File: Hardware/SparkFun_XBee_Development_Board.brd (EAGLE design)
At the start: 45.7 x 63.5 mm, 138 parts, among them J1 USB Female Type C Connector, J3 USB Female Type C Connector, J4 QWIIC_RIGHT_ANGLE, Q2 3.1A/30V/105mΩ, U1 FSUSB30MUX_MSOP10, U2 AP63203, U3 ESD Diode, U5 ESD Diode, U7 FT231XS

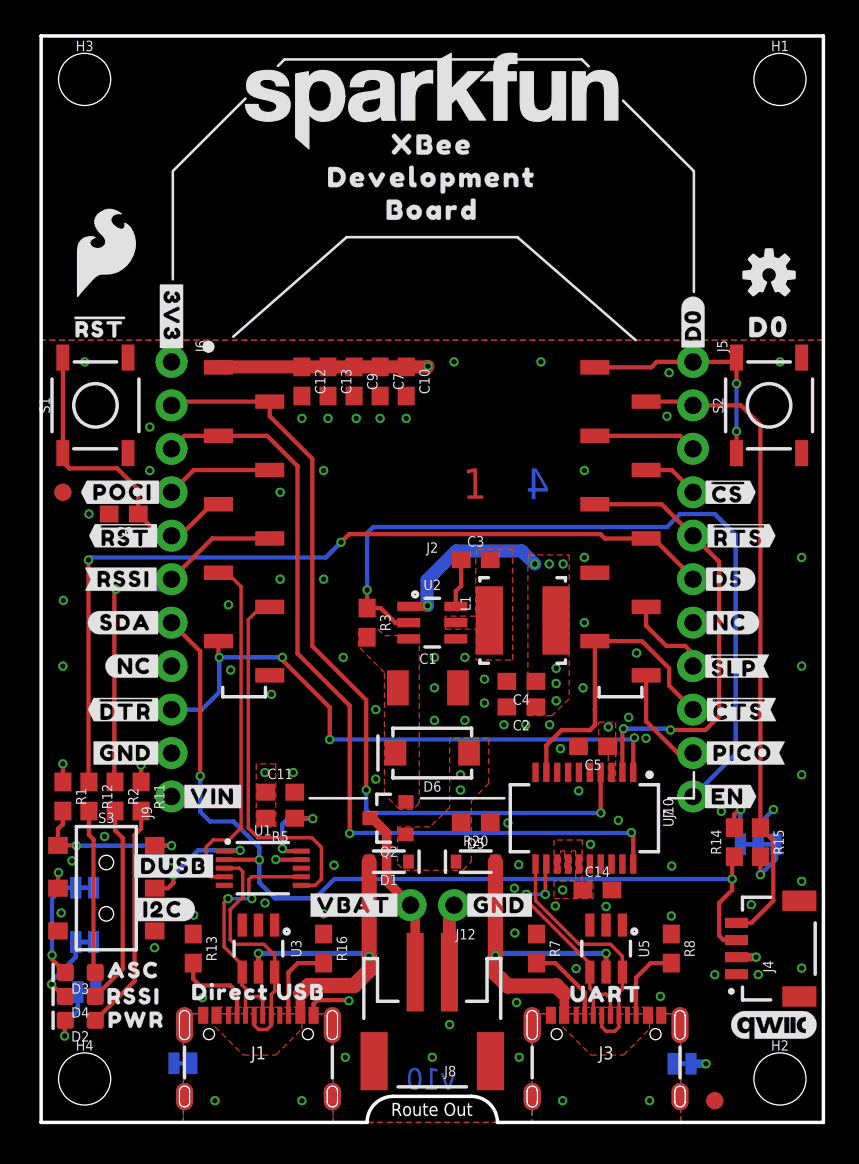
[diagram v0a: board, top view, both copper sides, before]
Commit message: Adds LED and Charging circuit - all routed (but not optimized
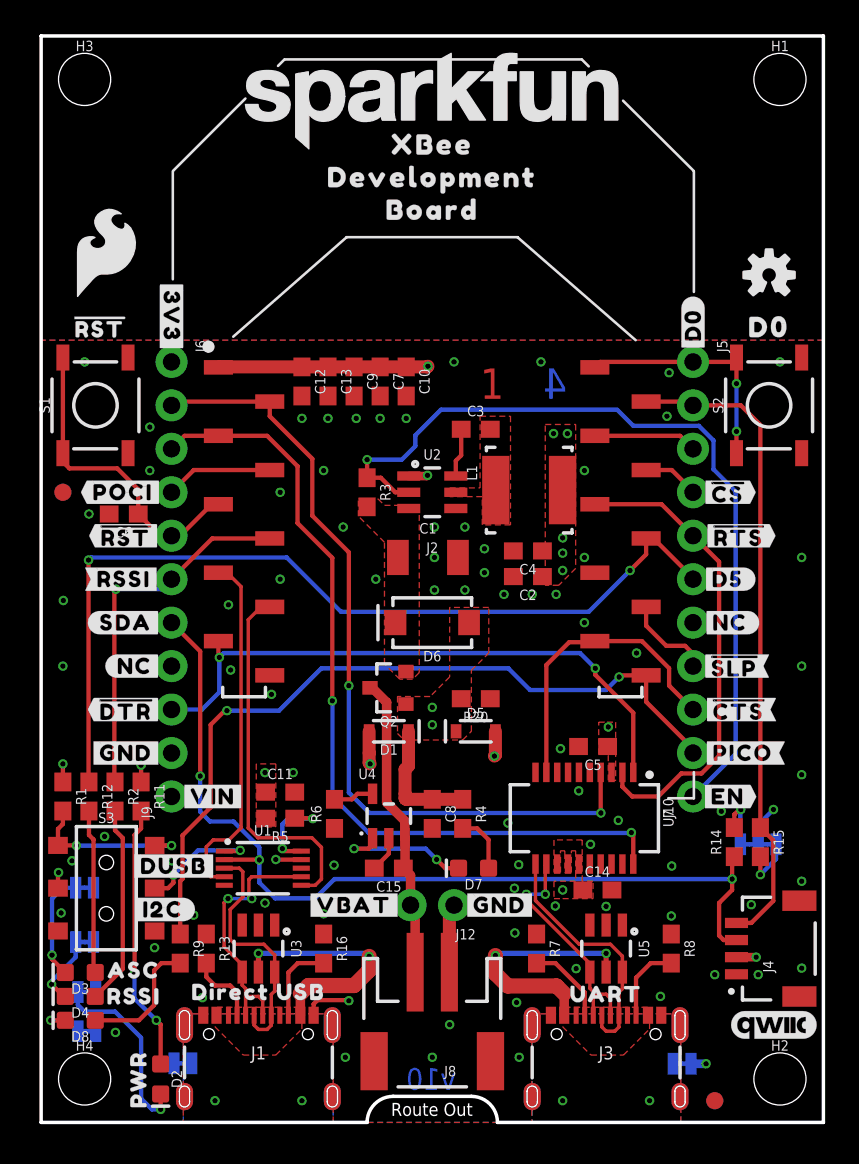
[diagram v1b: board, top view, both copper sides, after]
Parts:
- added C15, C8: 4.7uF, SparkFun-Capacitors:0603
- added D7, D8: Yellow, SparkFun-LED:LED-0603
- added IO4LED: JUMPER-SMT_2_NC_TRACE_SILK, SparkFun-Jumpers:SMT-JUMPER_2_NC_TRACE_SILK
- added R4: 4.7k, SparkFun-Resistors:0603
- added R6: 2.0k, SparkFun-Resistors:0603
- added R9: 2.2k, SparkFun-Resistors:0603
- added U4: MCP73831, SparkFun-IC-Power:SOT23-5
- moved C4 7.63 mm to (28.4, 33.4)
- moved C2 7.63 mm to (28.4, 31.9)
- moved L1 7.63 mm to (28.6, 37.0)
- moved C1 7.62 mm to (22.6, 33.0)
- moved D6 7.62 mm to (22.9, 29.2)
- moved D1 7.62 mm to (20.3, 22.9)
- moved D5 7.62 mm to (25.4, 22.9)
- moved C3 7.62 mm to (25.4, 40.5)
- moved Q2 7.62 mm to (20.3, 25.4)
- moved R3 7.62 mm to (19.1, 36.8)
- moved U2 7.62 mm to (22.9, 36.8)
- moved R20 7.24 mm to (25.4, 24.8)
- moved D2 5.82 mm to (6.99, 2.54), turned to 270 degrees
- moved U$42 3.48 mm to (5.69, 2.51), turned to 90 degrees
- moved R13 0.76 mm to (9.65, 10.2)
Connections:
- new net N$10: D7.A, R4.2
- new net N$17: D8.A, R9.2
- new net N$6: R6.2, U4.5
- new net N$9: D7.C, U4.1
- new net RLED1: D8.C, IO4LED.2
- net D4/SPI_PICO: now also R9.1
- net GND: now also C15.2, C8.2, IO4LED.1, R6.1, U4.2
- net VIN: now also C8.1, R4.1, U4.4
- net V_BATT: now also C15.1, U4.3
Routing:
- net D4/SPI_PICO: track 6.20 -> 46.4 mm, vias 0 -> 2
- net VIN: track 17.4 -> 26.8 mm
- net 3.3V: track 27.8 -> 19.0 mm, vias 15 -> 14
- net N$9: track 0.00 -> 8.14 mm, vias 0 -> 2
- net V_BATT: track 10.2 -> 17.9 mm
- net V_USB_2: track 19.8 -> 27.5 mm, vias 2 -> 3
- net V_USB: track 19.9 -> 27.6 mm, vias 2 -> 3
- net N$17: track 0.00 -> 7.54 mm
- net PLED: track 3.82 -> 11.1 mm
- net N$10: track 0.00 -> 3.45 mm
- net D5/ASSOCIATE: track 50.1 -> 53.0 mm
- net EN: track 46.0 -> 48.8 mm
- net RLED1: track 0.00 -> 2.70 mm, vias 0 -> 1
- net N$6: track 0.00 -> 2.36 mm
- net N$7: track 13.3 -> 15.6 mm, vias 0 -> 2
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
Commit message: Some routing improvements
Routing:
- net VIN: track 26.8 -> 24.9 mm
- net EN: track 48.8 -> 49.5 mm
- net D6/!RTS!: track 27.7 -> 28.3 mm
- net GND: vias 81 -> 79

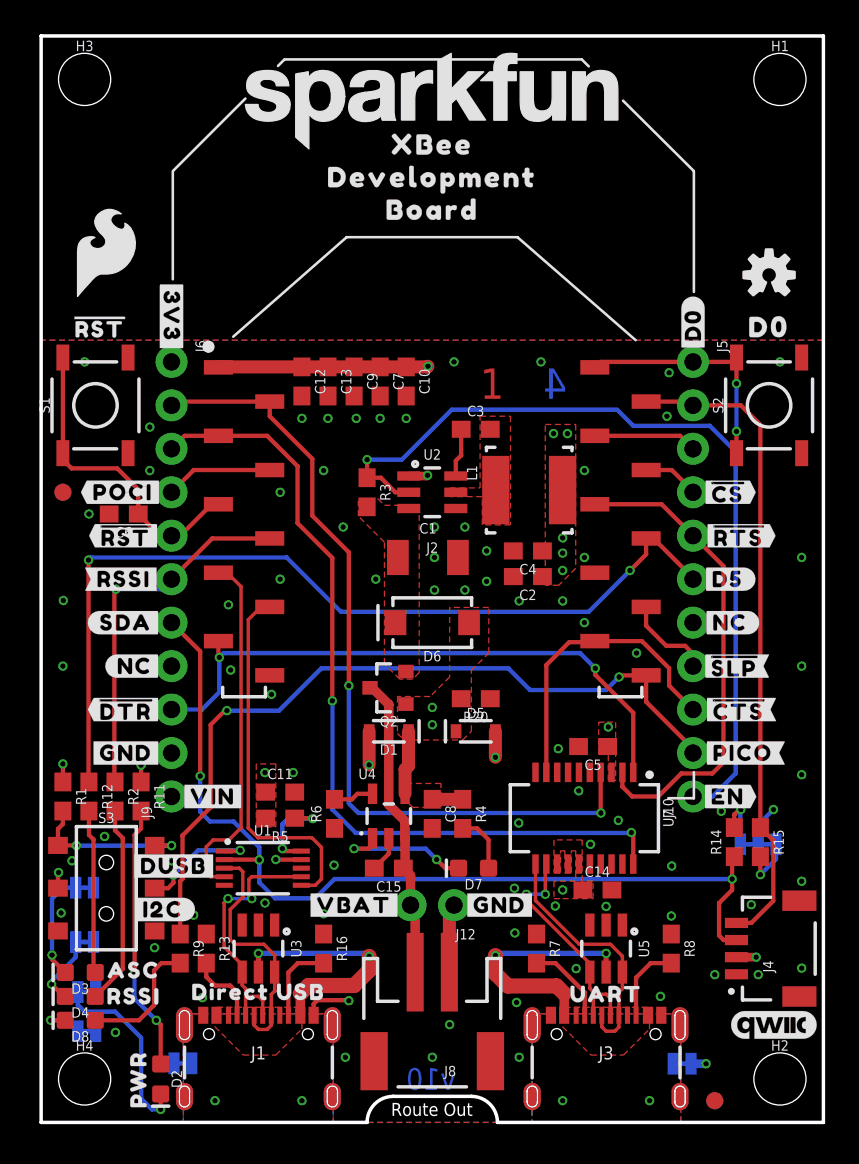
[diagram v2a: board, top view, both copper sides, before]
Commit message: Rolls version to v11 (applies to last commit)
* Adds silk
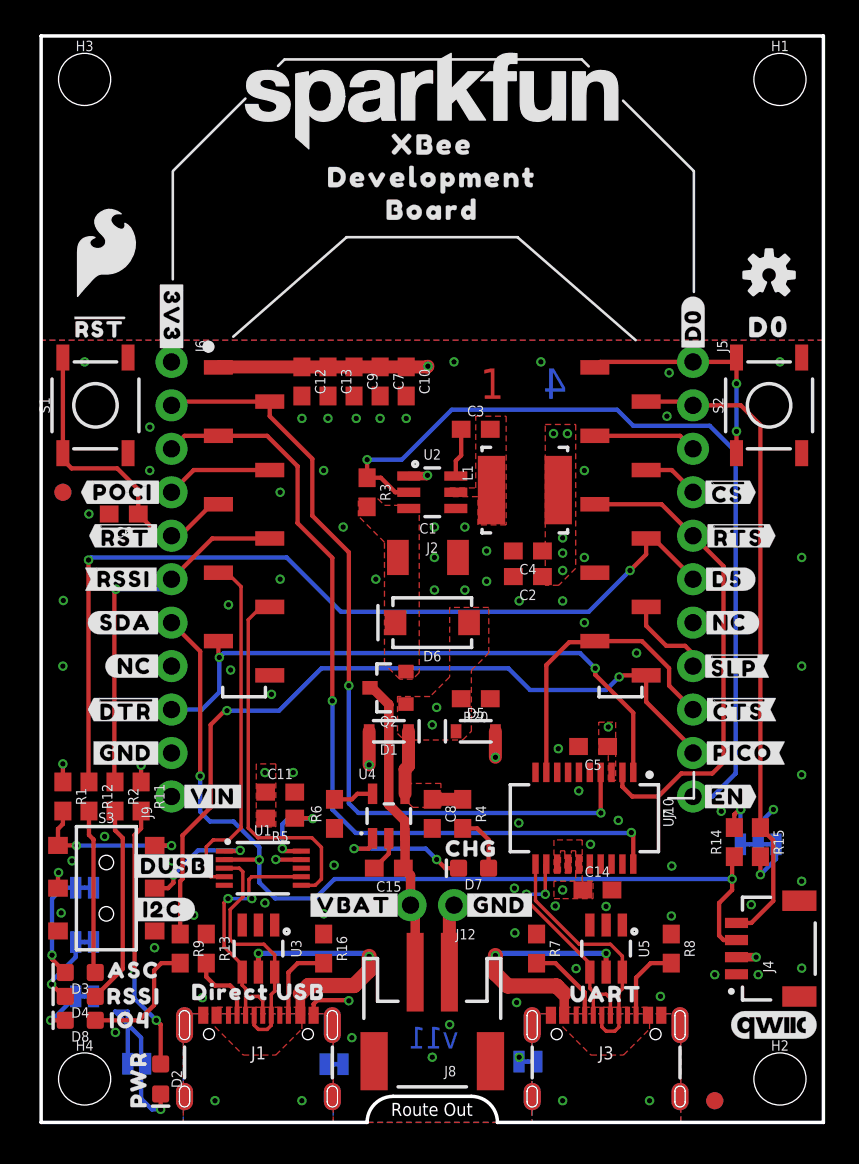
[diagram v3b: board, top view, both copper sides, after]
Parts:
- added U$19: (no value), pot:CHG47
- added U$33: (no value), pot:IO46
- added U$59: (no value), top:#IOLED#23
- U$35: device top:#SHLD#30 -> top:#SHLD#740
- U$36: device top:#SHLD1#31 -> top:#SHLD1#741
- moved SHLD 9.02 mm to (28.4, 3.56), turned to 180 degrees
- moved SHLD1 8.84 mm to (17.1, 3.40), turned to 0 degrees
- moved U$36 8.76 mm to (20.8, 3.30)
- moved U$54 5.18 mm to (9.02, 3.43)
- moved PLED 5.11 mm to (5.59, 3.43)
- moved U$35 2.16 mm to (31.9, 3.56)
- moved IO4LED 2.04 mm to (2.54, 7.37)
- moved L1 0.25 mm to (28.3, 37.0)
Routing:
- net GND: track 11.3 -> 10.4 mm, vias 79 -> 78
- net PLED: track 11.1 -> 11.8 mm
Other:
- board text added: "v11"
- board text removed: "v10"

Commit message: Changes silk on IOLED jumper
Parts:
- renumbered IO4LED to IOLED
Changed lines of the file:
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@@
 <attribute name="VALUE" x="7.366" y="10.16" size="0.6096" layer="27" font="vector" ratio="20" rot="R270" align="top-center"/>
 </element>
-<element name="IO4LED" library="SparkFun-Jumpers" package="SMT-JUMPER_2_NC_TRACE_SILK" package3d_urn="urn:adsk.eagle:package:39281/1" value="JUMPER-SMT_2_NC_TRACE_SILK" x="2.54" y="7.366" smashed="yes" rot="MR0">
+<element name="IOLED" library="SparkFun-Jumpers" package="SMT-JUMPER_2_NC_TRACE_SILK" package3d_urn="urn:adsk.eagle:package:39281/1" value="JUMPER-SMT_2_NC_TRACE_SILK" x="2.54" y="7.366" smashed="yes" rot="MR0">
 <attribute name="NAME" x="2.54" y="8.509" size="0.6096" layer="26" font="vector" ratio="20" rot="MR0" align="bottom-center"/>
 <attribute name="VALUE" x="2.54" y="6.223" size="0.6096" layer="28" font="vector" ratio="20" rot="MR0" align="top-center"/>
@@
 <contactref element="C8" pad="2"/>
 <contactref element="R6" pad="1"/>
-<contactref element="IO4LED" pad="1"/>
+<contactref element="IOLED" pad="1"/>
 <via x="22.987" y="34.798" extent="1-16" drill="0.3048"/>
 <wire x1="19.47" y1="14.859" x2="20.32" y2="15.709" width="0.254" layer="1"/>
@@
 </signal>
 <signal name="RLED1">
-<contactref element="IO4LED" pad="2"/>
+<contactref element="IOLED" pad="2"/>
 <contactref element="D8" pad="C"/>
 <wire x1="2.0193" y1="7.366" x2="0.6223" y2="5.969" width="0.254" layer="16"/>

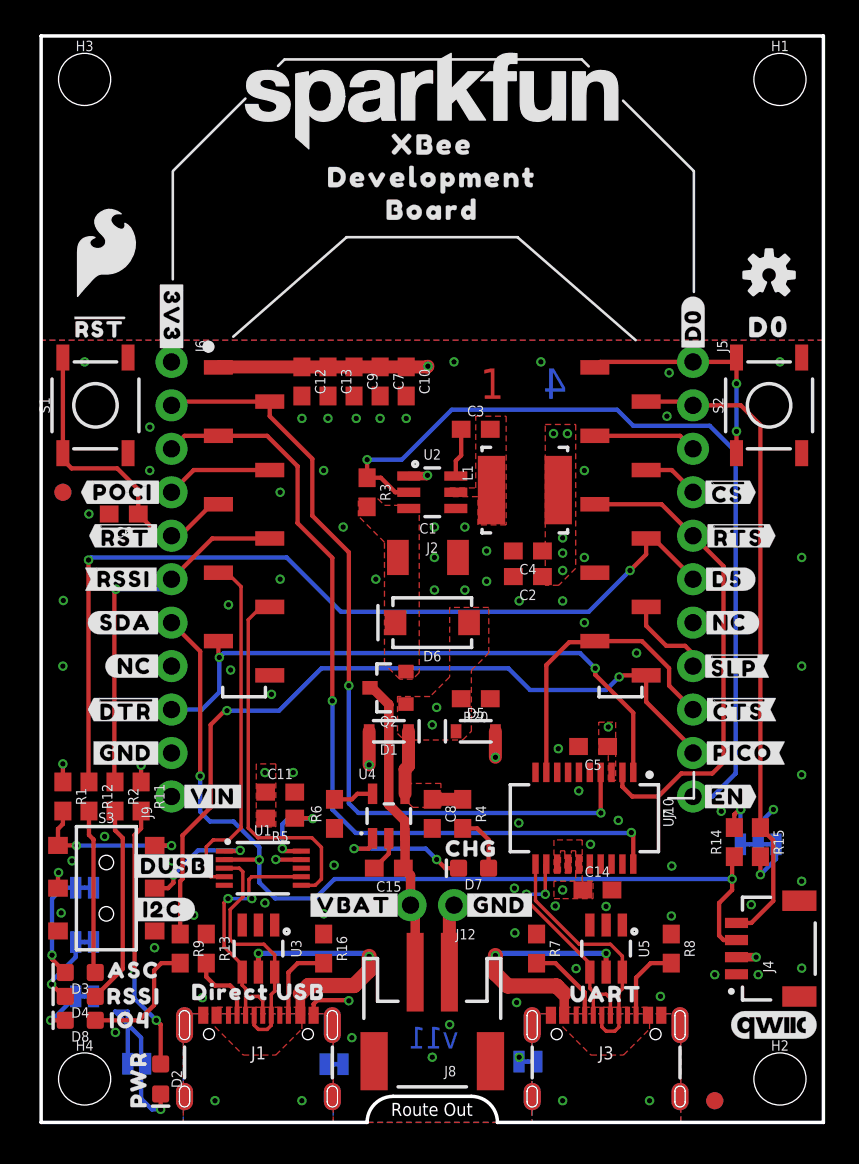
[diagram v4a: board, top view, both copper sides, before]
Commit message: Swaps yellow user LED for a green one
* Improves copper pour
* Fixes some whacky traces
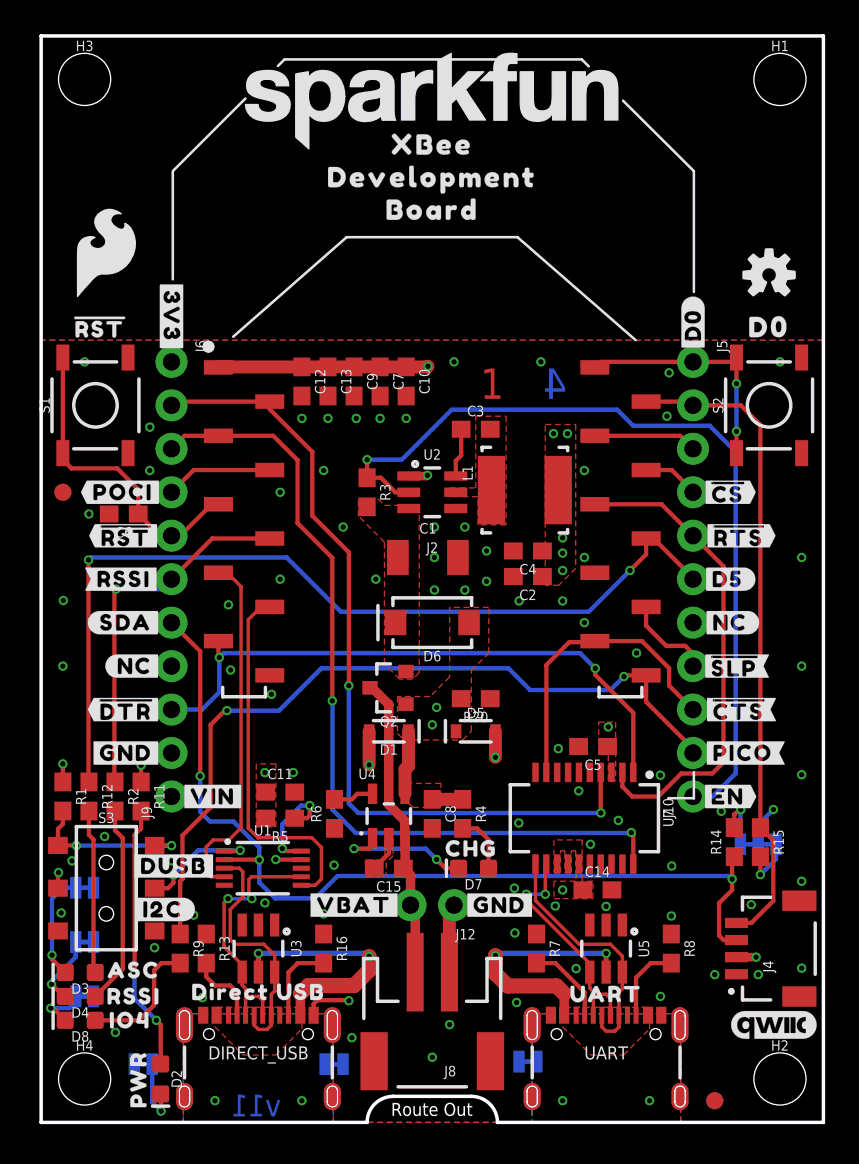
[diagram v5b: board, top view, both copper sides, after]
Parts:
- D8: value Yellow -> GREEN
- R11: value 1k -> 4.7k
- R9: value 2.2k -> 330
- moved U$54 0.43 mm to (9.45, 3.43)
- moved PLED 0.38 mm to (5.97, 3.40), turned to 180 degrees
- renumbered J1 to DIRECT_USB, J3 to UART
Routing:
- net PLED: track 11.8 -> 3.97 mm
- net N$3: track 5.57 -> 6.17 mm
